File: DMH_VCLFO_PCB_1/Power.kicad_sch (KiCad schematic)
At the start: 14 parts, among them J0 Conn_01x01, J100 IDC_02x05, J101 IDC_02x08

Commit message: schematic design in progress
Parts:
- removed C5: 47uF, Capacitor_THT:CP_Radial_D4.0mm_P1.50mm, symbol Device:C_Polarized
- removed C6: 100nF, Capacitor_THT:C_Disc_D4.3mm_W1.9mm_P5.00mm, symbol Device:C
- removed D3, D4, D5: SB140, Diode_THT:D_DO-41_SOD81_P10.16mm_Horizontal, symbol Diode:SB140
- removed J101: IDC_02x08, SynthStuff:IDC-Header_2x08_P2.54mm_Vertical_Eurorack, symbol SynthStuff:Eurorack_Power_Connector_16Pin
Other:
- note removed: "Delete what's not needed!"

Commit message: Ready for breadboarding
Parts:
- removed C3, C4: 100nF, Capacitor_THT:C_Disc_D4.3mm_W1.9mm_P5.00mm, symbol Device:C
- added D3, D4: LM4040LP-5, Package_TO_SOT_THT:TO-92_Inline, symbol Reference_Voltage:LM4040LP-5
- added R1, R2: 470R, Resistor_THT:R_Axial_DIN0207_L6.3mm_D2.5mm_P7.62mm_Horizontal, symbol Device:R_US
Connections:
- net +12V: now also R1.1
- net -12V: now also R2.1
- net GND: now also D3.3 (A), D4.2 (K)
- new net +5V: D3.2 (K), R1.2
- new net -5V: D4.3 (A), R2.2

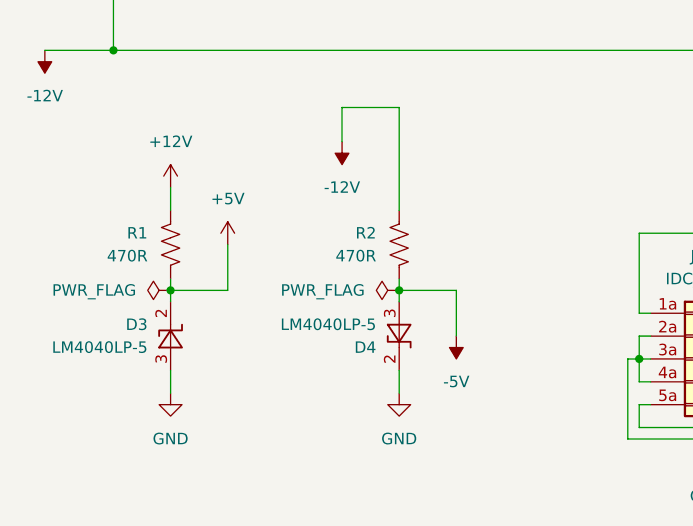
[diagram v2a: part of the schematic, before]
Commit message: Fixed issue with polarity selector
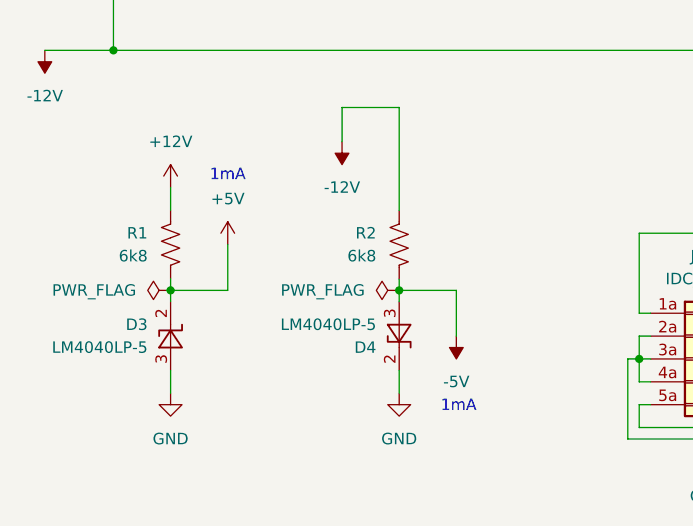
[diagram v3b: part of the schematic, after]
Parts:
- R1, R2: value 470R -> 6k8
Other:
- note added: "1mA"
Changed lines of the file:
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@@
 		(comment 1 "PCB for 10cm Kosmo format synthesizer module")
+	)
+	(text "1mA"
+		(exclude_from_sim no)
+		(at 63.754 185.674 0)
+		(effects
+			(font
+				(size 1.27 1.27)
+			)
+		)
+	)
+	(text "1mA"
+		(exclude_from_sim no)
+		(at 38.1 160.02 0)
+		(effects
+			(font
+				(size 1.27 1.27)
+			)
+		)
 	)
 	(junction
@@
 			)
 		)
-		(property "Value" "470R"
+		(property "Value" "6k8"
 			(at 29.21 168.9099 0)
 			(effects
@@
 			)
 		)
-		(property "Value" "470R"
+		(property "Value" "6k8"
 			(at 54.61 168.9099 0)
 			(effects
